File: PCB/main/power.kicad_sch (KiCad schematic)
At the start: 0 parts

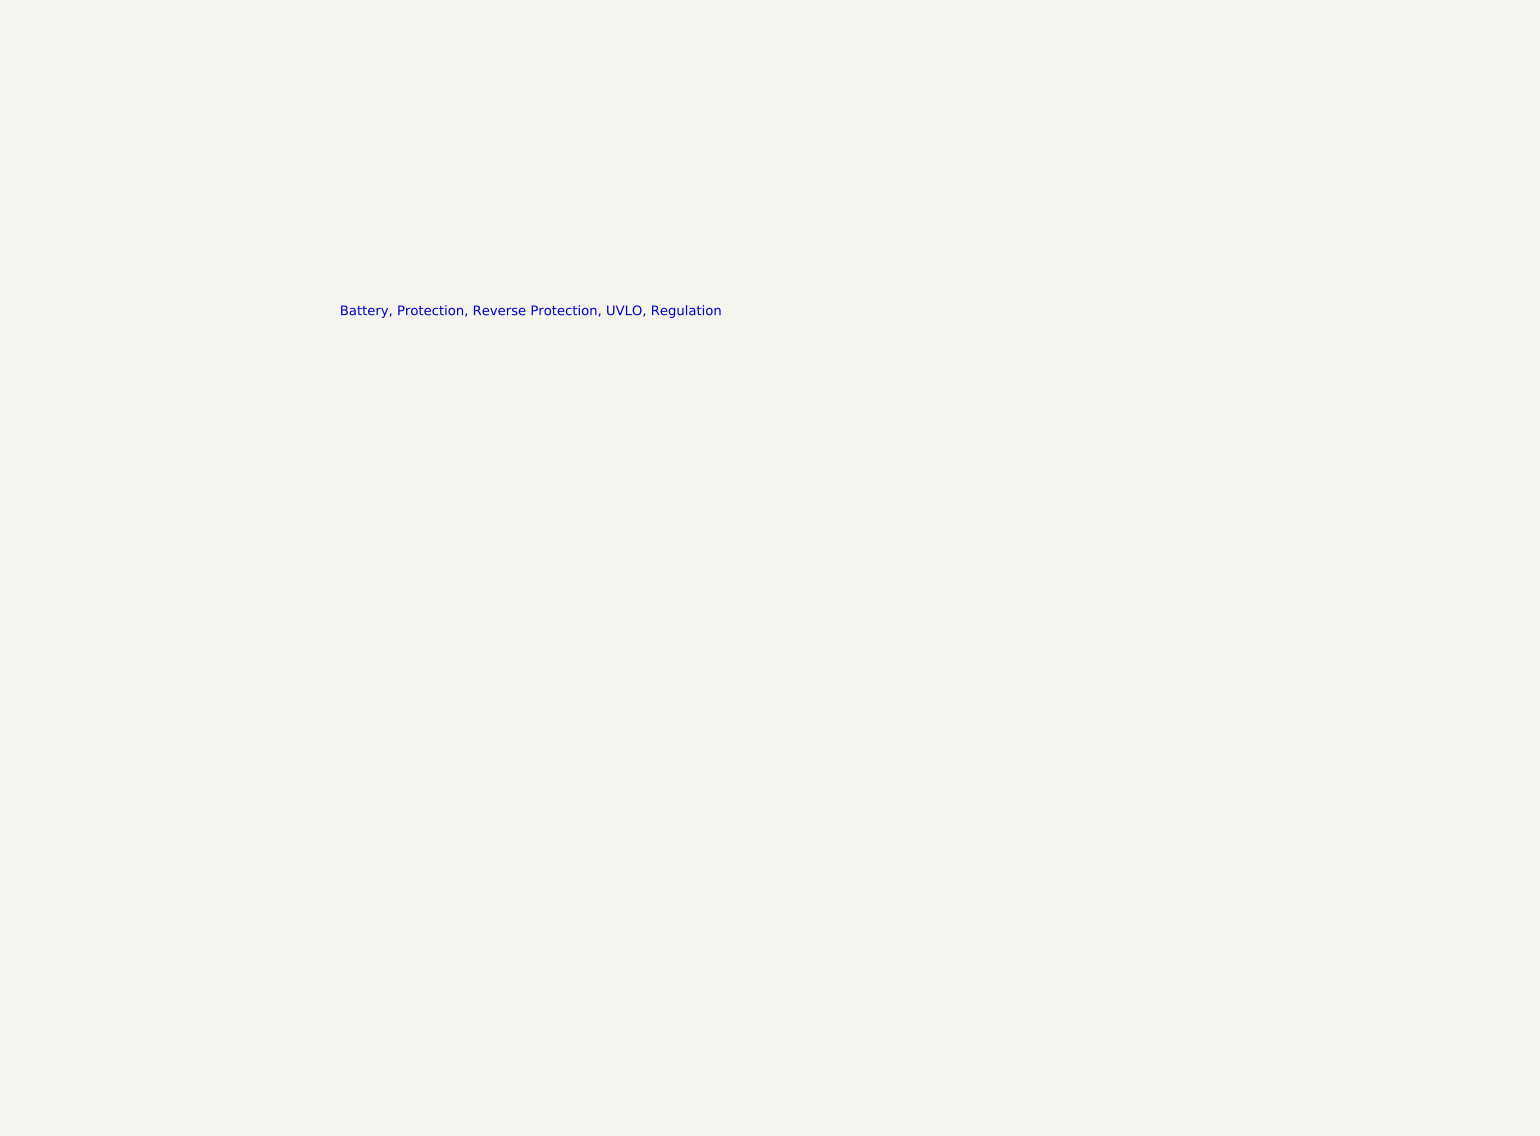
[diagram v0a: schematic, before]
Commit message: updated power schematic
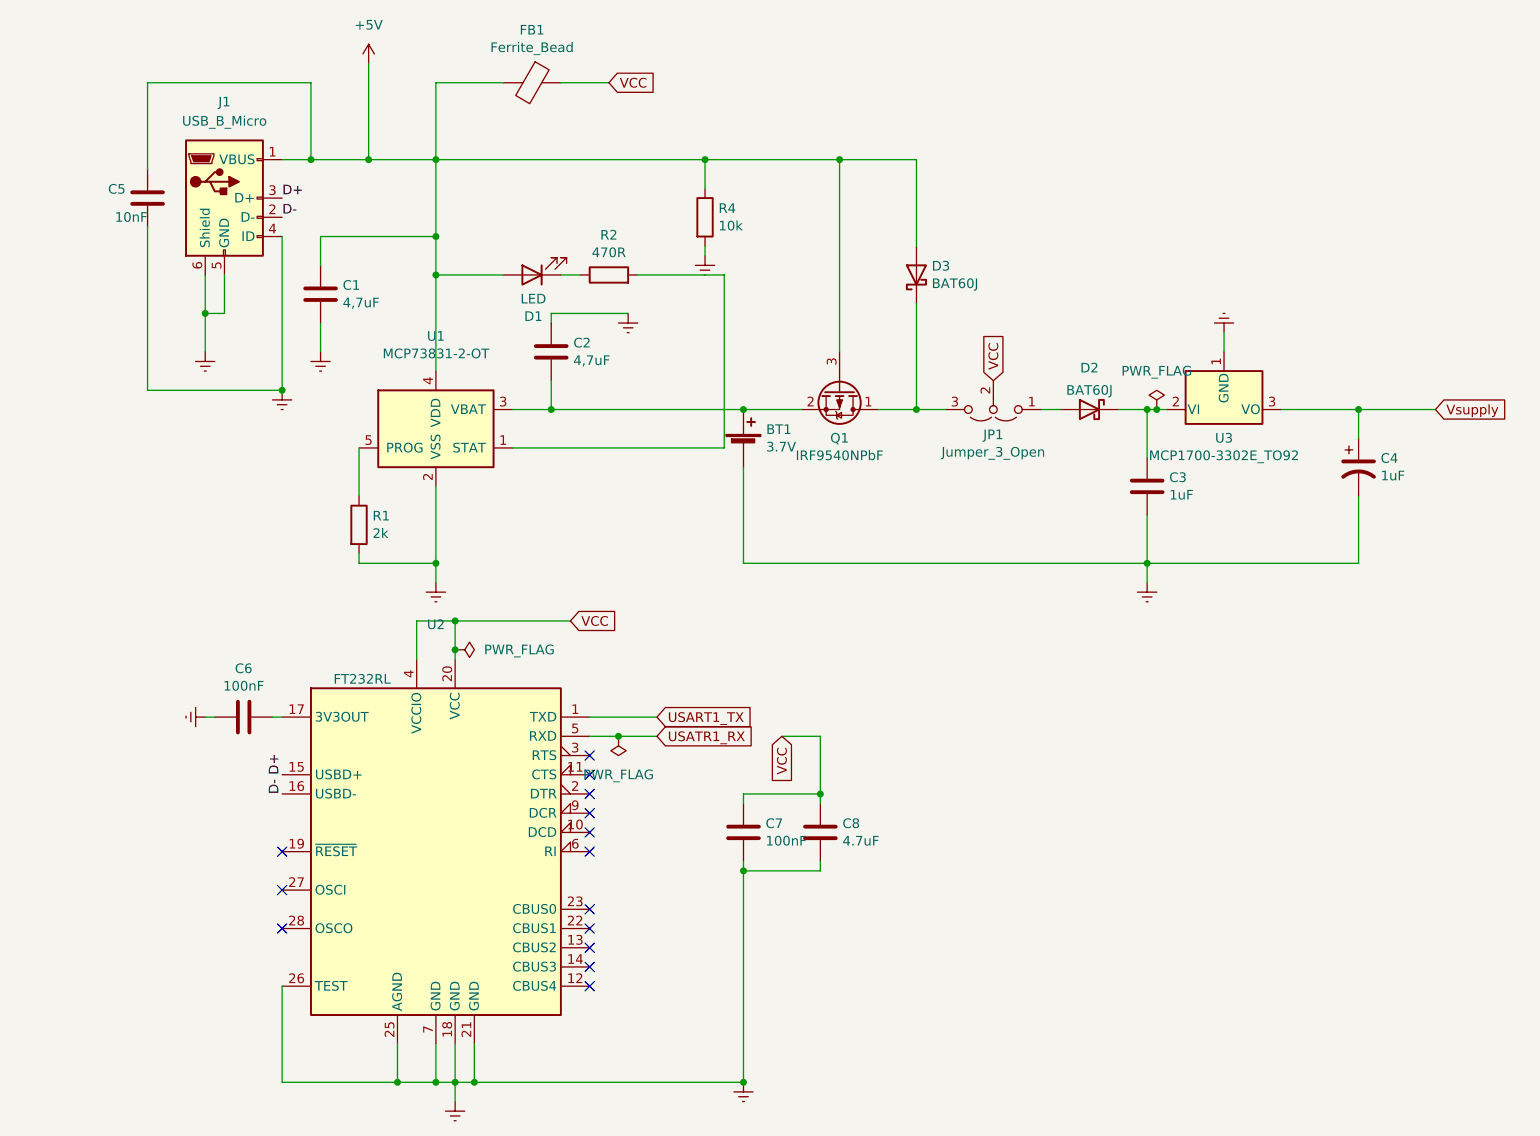
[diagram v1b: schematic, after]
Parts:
- added BT1: 3.7V, Battery:BatteryHolder_Keystone_1042_1x18650, symbol Device:Battery_Cell
- added C1, C2: 4,7uF, CAP4UF7:CAPC1608X90N, symbol Device:C
- added C3: 1uF, CAP1UF:CAPC1608X90N, symbol Device:C
- added C4: 1uF, CAP1UF:CAPC1608X90N, symbol EEE3088_PROJECT-rescue:CP1-Device
- added C5: 10nF, Capacitor_SMD:C_0402_1005Metric, symbol Device:C
- added C6, C7: 100nF, CAP100NF:CAPC1608X90N, symbol Device:C
- added C8: 4.7uF, CAP4UF7:CAPC1608X90N, symbol Device:C
- added D1: LED, MYLED:LEDC1608X70N, symbol Device:LED
- added D2: BAT60J, Diode_SMD:D_SOD-323, symbol Device:D_Schottky
- added D3: BAT60J, Diode_SMD:D_SOD-323, symbol Diode:BAT60A
- added FB1: Ferrite_Bead, FERRITE_BEAD:BEADC1608X95N, symbol EEE3088_PROJECT-rescue:Ferrite_Bead-Device
- added J1: USB_B_Micro, USB:MICROXNJ, symbol Connector:USB_B_Micro
- added JP1: Jumper_3_Open, Jumper:SolderJumper-3_P1.3mm_Open_Pad1.0x1.5mm_NumberLabels, symbol EEE3088_PROJECT-rescue:Jumper_3_Open-Jumper
- added Q1: IRF9540NPbF, MYMOSFET:TO254P469X1042X1967-3P, symbol Device:Q_PMOS_DSG
- added R1: 2k, R2K:RESC1005X35N, symbol Device:R
- added R2: 470R, R470R:RESC1608X55N, symbol Device:R
- added R4: 10k, R10K:RESC1608X55N, symbol Device:R
- added U1: MCP73831-2-OT, Package_TO_SOT_SMD:SOT-23-5, symbol Battery_Management:MCP73831-2-OT
- added U2: FT232RL, Package_SO:SSOP-28_5.3x10.2mm_P0.65mm, symbol Interface_USB:FT232RL
- added U3: MCP1700-3302E_TO92, Package_TO_SOT_THT:TO-92_Inline, symbol Regulator_Linear:MCP1700-3302E_TO92
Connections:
- new net: R2.2, U1.1 (STAT)
- new net: BT1.1 (+), C2.2, Q1.2 (S), U1.3 (VBAT)
- new net: R1.1, U1.5 (PROG)
- new net: D1.1 (K), R2.1
- new net: C3.1, D2.1 (K), U3.2 (VI)
- new net: D2.2 (A), JP1.1 (A)
- new net: D3.1 (K), JP1.3 (B), Q1.1 (D)
- new net: C6.2, U2.17 (3V3OUT)
- new net +5V: C1.1, C5.2, D1.2 (A), D3.2 (A), FB1.2, J1.1 (VBUS), Q1.3 (G), R4.1, U1.4 (VDD)
- new net D+: J1.3 (D+), U2.15 (USBD+)
- new net D-: J1.2 (D-), U2.16 (USBD-)
- new net Earth: BT1.2 (-), C1.2, C2.1, C3.2, C4.2, C5.1, C6.1, C7.2, C8.2, J1.4 (ID), J1.5 (GND), J1.6 (Shield), R1.2, R4.2, U1.2 (VSS), U2.18 (GND), U2.21 (GND), U2.25 (AGND), U2.26 (TEST), U2.7 (GND), U3.1 (GND)
- new net USART1_TX: U2.1 (TXD)
- new net USATR1_RX: U2.5 (RXD)
- new net VCC: C7.1, C8.1, FB1.1, JP1.2 (C), U2.20 (VCC), U2.4 (VCCIO)
- new net Vsupply: C4.1, U3.3 (VO)
- no-connect marks 0 -> 14
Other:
- note removed: "Battery, Protection, Reverse Protection, UVLO, Regulation"
- company: (none) -> UCT
- title: (none) -> Power submodule

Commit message: assigned new footprints
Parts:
- C1, C2, C8: footprint CAP4UF7:CAPC1608X90N -> SamacSys_Parts:CAPC1608X90N
- C3, C4: footprint CAP1UF:CAPC1608X90N -> SamacSys_Parts:CAPC1608X90N
- C5: footprint Capacitor_SMD:C_0402_1005Metric -> SamacSys_Parts:CAPC1608X90N
- C6, C7: footprint CAP100NF:CAPC1608X90N -> SamacSys_Parts:CAPC1608X90N
- D1: footprint MYLED:LEDC1608X70N -> SamacSys_Parts:LEDC1608X70N
- FB1: footprint FERRITE_BEAD:BEADC1608X95N -> SamacSys_Parts:BEADC1608X95N
- J1: footprint USB:MICROXNJ -> SamacSys_Parts:MICROXNJ
- Q1: footprint MYMOSFET:TO254P469X1042X1967-3P -> SamacSys_Parts:TO254P469X1042X1967-3P
- R1: footprint R2K:RESC1005X35N -> SamacSys_Parts:RESC1005X35N
- R2: footprint R470R:RESC1608X55N -> SamacSys_Parts:RESC1608X55N
- R4: footprint R10K:RESC1608X55N -> SamacSys_Parts:RESC1608X55N
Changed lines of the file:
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@@
     (property "Reference" "D1" (id 0) (at 147.4978 89.3064 0))
     (property "Value" "LED" (id 1) (at 147.4978 86.995 0))
-    (property "Footprint" "MYLED:LEDC1608X70N" (id 2) (at 147.32 83.82 0)
+    (property "Footprint" "SamacSys_Parts:LEDC1608X70N" (id 2) (at 147.32 83.82 0)
       (effects (font (size 1.27 1.27)) hide)
     )
@@
     (property "Reference" "R2" (id 0) (at 157.48 78.5622 90))
     (property "Value" "470R" (id 1) (at 157.48 80.8736 90))
-    (property "Footprint" "R470R:RESC1608X55N" (id 2) (at 157.48 85.598 90)
+    (property "Footprint" "SamacSys_Parts:RESC1608X55N" (id 2) (at 157.48 85.598 90)
       (effects (font (size 1.27 1.27)) hide)
     )
@@
       (effects (font (size 1.27 1.27)) (justify left))
     )
-    (property "Footprint" "R2K:RESC1005X35N" (id 2) (at 122.682 116.84 90)
+    (property "Footprint" "SamacSys_Parts:RESC1005X35N" (id 2) (at 122.682 116.84 90)
       (effects (font (size 1.27 1.27)) hide)
     )
@@
       (effects (font (size 1.27 1.27)) (justify left))
     )
-    (property "Footprint" "CAP1UF:CAPC1608X90N" (id 2) (at 229.5652 115.57 0)
+    (property "Footprint" "SamacSys_Parts:CAPC1608X90N" (id 2) (at 229.5652 115.57 0)
       (effects (font (size 1.27 1.27)) hide)
     )
@@
       (effects (font (size 1.27 1.27)) (justify left))
     )
-    (property "Footprint" "CAP4UF7:CAPC1608X90N" (id 2) (at 120.3452 90.17 0)
+    (property "Footprint" "SamacSys_Parts:CAPC1608X90N" (id 2) (at 120.3452 90.17 0)
       (effects (font (size 1.27 1.27)) hide)
     )
@@
       (effects (font (size 1.27 1.27)) (justify left))
     )
-    (property "Footprint" "CAP4UF7:CAPC1608X90N" (id 2) (at 150.8252 97.79 0)
+    (property "Footprint" "SamacSys_Parts:CAPC1608X90N" (id 2) (at 150.8252 97.79 0)
       (effects (font (size 1.27 1.27)) hide)
     )
@@
       (effects (font (size 1.27 1.27)) (justify left))
     )
-    (property "Footprint" "CAP1UF:CAPC1608X90N" (id 2) (at 256.54 109.22 0)
+    (property "Footprint" "SamacSys_Parts:CAPC1608X90N" (id 2) (at 256.54 109.22 0)
       (effects (font (size 1.27 1.27)) hide)
     )
@@
       (effects (font (size 1.27 1.27)) (justify left))
     )
-    (property "Footprint" "R10K:RESC1608X55N" (id 2) (at 168.402 76.2 90)
+    (property "Footprint" "SamacSys_Parts:RESC1608X55N" (id 2) (at 168.402 76.2 90)
       (effects (font (size 1.27 1.27)) hide)
     )
@@
     (property "Reference" "Q1" (id 0) (at 187.96 105.3846 90))
     (property "Value" "IRF9540NPbF" (id 1) (at 187.96 107.696 90))
-    (property "Footprint" "MYMOSFET:TO254P469X1042X1967-3P" (id 2) (at 190.5 104.14 0)
+    (property "Footprint" "SamacSys_Parts:TO254P469X1042X1967-3P" (id 2) (at 190.5 104.14 0)
       (effects (font (size 1.27 1.27)) hide)
     )
@@
     (property "Reference" "C6" (id 0) (at 109.22 135.8392 90))
     (property "Value" "100nF" (id 1) (at 109.22 138.1506 90))
-    (property "Footprint" "CAP100NF:CAPC1608X90N" (id 2) (at 113.03 141.2748 0)
+    (property "Footprint" "SamacSys_Parts:CAPC1608X90N" (id 2) (at 113.03 141.2748 0)
       (effects (font (size 1.27 1.27)) hide)
     )
@@
       (effects (font (size 1.27 1.27)) (justify right))
     )
-    (property "Footprint" "Capacitor_SMD:C_0402_1005Metric" (id 2) (at 97.4852 69.85 0)
+    (property "Footprint" "SamacSys_Parts:CAPC1608X90N" (id 2) (at 97.4852 69.85 0)
       (effects (font (size 1.27 1.27)) hide)
     )
@@
       (effects (font (size 1.27 1.27)) (justify left))
     )
-    (property "Footprint" "CAP100NF:CAPC1608X90N" (id 2) (at 176.2252 161.29 0)
+    (property "Footprint" "SamacSys_Parts:CAPC1608X90N" (id 2) (at 176.2252 161.29 0)
       (effects (font (size 1.27 1.27)) hide)
     )
@@
       (effects (font (size 1.27 1.27)) (justify left))
     )
-    (property "Footprint" "CAP4UF7:CAPC1608X90N" (id 2) (at 186.3852 161.29 0)
+    (property "Footprint" "SamacSys_Parts:CAPC1608X90N" (id 2) (at 186.3852 161.29 0)
       (effects (font (size 1.27 1.27)) hide)
     )
@@
     (property "Reference" "FB1" (id 0) (at 147.32 51.4604 90))
     (property "Value" "Ferrite_Bead" (id 1) (at 147.32 53.7718 90))
-    (property "Footprint" "FERRITE_BEAD:BEADC1608X95N" (id 2) (at 147.32 56.642 90)
+    (property "Footprint" "SamacSys_Parts:BEADC1608X95N" (id 2) (at 147.32 56.642 90)
       (effects (font (size 1.27 1.27)) hide)
     )
@@
     (property "Reference" "J1" (id 0) (at 106.68 60.96 0))
     (property "Value" "USB_B_Micro" (id 1) (at 106.68 63.5 0))
-    (property "Footprint" "USB:MICROXNJ" (id 2) (at 110.49 74.93 0)
+    (property "Footprint" "SamacSys_Parts:MICROXNJ" (id 2) (at 110.49 74.93 0)
       (effects (font (size 1.27 1.27)) hide)
     )
@@
     )
     (path "/00000000-0000-0000-0000-00006225de26"
-      (reference "C1") (unit 1) (value "4,7uF") (footprint "CAP4UF7:CAPC1608X90N")
+      (reference "C1") (unit 1) (value "4,7uF") (footprint "SamacSys_Parts:CAPC1608X90N")
     )
     (path "/00000000-0000-0000-0000-00006225e5d2"
-      (reference "C2") (unit 1) (value "4,7uF") (footprint "CAP4UF7:CAPC1608X90N")
+      (reference "C2") (unit 1) (value "4,7uF") (footprint "SamacSys_Parts:CAPC1608X90N")
     )
     (path "/00000000-0000-0000-0000-00006225032a"
-      (reference "C3") (unit 1) (value "1uF") (footprint "CAP1UF:CAPC1608X90N")
+      (reference "C3") (unit 1) (value "1uF") (footprint "SamacSys_Parts:CAPC1608X90N")
     )
     (path "/00000000-0000-0000-0000-000062266550"
-      (reference "C4") (unit 1) (value "1uF") (footprint "CAP1UF:CAPC1608X90N")
+      (reference "C4") (unit 1) (value "1uF") (footprint "SamacSys_Parts:CAPC1608X90N")
     )
     (path "/00000000-0000-0000-0000-000062307c35"
-      (reference "C5") (unit 1) (value "10nF") (footprint "Capacitor_SMD:C_0402_1005Metric")
+      (reference "C5") (unit 1) (value "10nF") (footprint "SamacSys_Parts:CAPC1608X90N")
     )
     (path "/00000000-0000-0000-0000-0000622f4aab"
-      (reference "C6") (unit 1) (value "100nF") (footprint "CAP100NF:CAPC1608X90N")
+      (reference "C6") (unit 1) (value "100nF") (footprint "SamacSys_Parts:CAPC1608X90N")
     )
     (path "/00000000-0000-0000-0000-00006232db0b"
-      (reference "C7") (unit 1) (value "100nF") (footprint "CAP100NF:CAPC1608X90N")
+      (reference "C7") (unit 1) (value "100nF") (footprint "SamacSys_Parts:CAPC1608X90N")
     )
     (path "/00000000-0000-0000-0000-00006232deab"
-      (reference "C8") (unit 1) (value "4.7uF") (footprint "CAP4UF7:CAPC1608X90N")
+      (reference "C8") (unit 1) (value "4.7uF") (footprint "SamacSys_Parts:CAPC1608X90N")
     )
     (path "/00000000-0000-0000-0000-00006221ee4c"
-      (reference "D1") (unit 1) (value "LED") (footprint "MYLED:LEDC1608X70N")
+      (reference "D1") (unit 1) (value "LED") (footprint "SamacSys_Parts:LEDC1608X70N")
     )
     (path "/00000000-0000-0000-0000-00006224b297"
@@
     )
     (path "/00000000-0000-0000-0000-000062372cae"
-      (reference "FB1") (unit 1) (value "Ferrite_Bead") (footprint "FERRITE_BEAD:BEADC1608X95N")
+      (reference "FB1") (unit 1) (value "Ferrite_Bead") (footprint "SamacSys_Parts:BEADC1608X95N")
     )
     (path "/f49b8522-b24a-41ad-a3b1-8dca1ceb9a62"
-      (reference "J1") (unit 1) (value "USB_B_Micro") (footprint "USB:MICROXNJ")
+      (reference "J1") (unit 1) (value "USB_B_Micro") (footprint "SamacSys_Parts:MICROXNJ")
     )
     (path "/00000000-0000-0000-0000-000062332161"
@@
     )
     (path "/00000000-0000-0000-0000-0000622c2216"
-      (reference "Q1") (unit 1) (value "IRF9540NPbF") (footprint "MYMOSFET:TO254P469X1042X1967-3P")
+      (reference "Q1") (unit 1) (value "IRF9540NPbF") (footprint "SamacSys_Parts:TO254P469X1042X1967-3P")
     )
     (path "/00000000-0000-0000-0000-00006222005f"
-      (reference "R1") (unit 1) (value "2k") (footprint "R2K:RESC1005X35N")
+      (reference "R1") (unit 1) (value "2k") (footprint "SamacSys_Parts:RESC1005X35N")
     )
     (path "/00000000-0000-0000-0000-00006221f4c9"
-      (reference "R2") (unit 1) (value "470R") (footprint "R470R:RESC1608X55N")
+      (reference "R2") (unit 1) (value "470R") (footprint "SamacSys_Parts:RESC1608X55N")
     )
     (path "/00000000-0000-0000-0000-0000622b9939"
-      (reference "R4") (unit 1) (value "10k") (footprint "R10K:RESC1608X55N")
+      (reference "R4") (unit 1) (value "10k") (footprint "SamacSys_Parts:RESC1608X55N")
     )
     (path "/00000000-0000-0000-0000-00006221d448"
